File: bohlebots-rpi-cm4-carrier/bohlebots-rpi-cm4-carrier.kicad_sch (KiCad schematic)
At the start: 28 parts, among them J1 SI-46001-F, J2 power_reference, J3 IO_Conn_02x05, J4 I2C_Conn_1x04, K1 Kicker, T1 Taster_LED, T2 Taster_LED, U1 Compute_Module_4_Connectors, U2 USB_Conn_01x05_Pin, X1 Miromatch

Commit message: Added esd protection TODO: find fitting tvs diode (tht) 2p, 4p
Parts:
- added U2: TPD2EUSB30, Package_TO_SOT_SMD:Texas_DRT-3, symbol Power_Protection:TPD2EUSB30
- added U5: TPD4EUSB30, Package_SON:USON-10_2.5x1.0mm_P0.5mm, symbol CM4IO:TPD4EUSB30
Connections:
- net GND: now also U2.3 (GND), U5.3 (GND), U5.8 (GND)
- net USB_N: now also U2.2 (D-)
- net USB_P: now also U2.1 (D+)
- net USB_OTG: now reaches U1.101 (USB_OTG_ID)
- net USB_OTG: now also J3.9 (USB_OTG)
- net RUN_PG: no longer names the net of U1.92 (RUN_PG)
- net RUN_PG: no longer J3.9 (RUN_PG)
- new net TRD0_N: U5.4 (D2+), U5.7
- new net TRD0_P: U5.5 (D2-), U5.6
- new net TRD1_N: U5.2 (D1-), U5.9
- new net TRD1_P: U5.1 (D1+), U5.10
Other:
- note removed: "drive low with 220R to reset"
- moved on the sheet: J3, J4

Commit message: Added tsv diodes.
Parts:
- removed U2: TPD2EUSB30, Package_TO_SOT_SMD:Texas_DRT-3, symbol Power_Protection:TPD2EUSB30
- added U3: DT1446-04SO-7, bohlebots-rpi-cm4-carrier:SOT26, symbol CM4IO:TPD4EUSB30
- U5: value TPD4EUSB30 -> DT1446-04SO-7; footprint Package_SON:USON-10_2.5x1.0mm_P0.5mm -> bohlebots-rpi-cm4-carrier:SOT26; Hersteller (none) -> Diodes Incorporated
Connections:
- net TRD0_N is gone; now on net USB_N: U5.4 (D2+), U5.7
- net 5V: now also U5.5 (VCC)
- net GND: now also U5.2 (GND), U3.2 (GND), U3.8 (GND); no longer U5.3 (GND)
- net RD_N: now also U3.1 (D1-), U3.9
- net RD_P: now also U3.10, U3.6
- net TD_N: now also U3.3 (D2-), U3.6
- net TD_P: now also U3.4 (D2+), U3.7
- net USB_P: now also U5.3 (D2-), U5.6
- removed net TRD0_P: U5.5 (D2-), U5.6
- net TRD1_N: no longer names the net of U5.9
- net TRD1_N: now also U5.1 (D1-); no longer U5.2 (D1-)
- net TRD1_P: no longer names the net of U5.10
- net TRD1_P: now also U5.6; no longer U5.1 (D1+)
- net USB_OTG renamed USB_OTG_ID
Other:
- moved on the sheet: C1, ESCON1, ESCON2, ESCON3, ESCON4, J1, J3, J4, JP1, JP2, JP3, JP4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

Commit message: Started routing.
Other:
- moved on the sheet: C1, J1, U2, U3, U5

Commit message: PCB Layout Update.
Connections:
- net USB_N: now also U5.1 (D1-), U5.9; no longer U5.4 (D2+), U5.7
- net USB_P: now also U5.10; no longer U5.3 (D2-)
- new net: U5.3 (D2-), U5.6
- new net: U5.4 (D2+), U5.7
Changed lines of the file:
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@@
     (effects (font (size 1.27 1.27)) (justify right bottom))
-  )
-  (label "USB_N" (at 265.43 104.14 0) (fields_autoplaced)
-    (effects (font (size 1.27 1.27)) (justify left bottom))
   )
   (label "PWM3" (at 120.65 59.69 0) (fields_autoplaced)
@@
     (effects (font (size 1.27 1.27)) (justify left bottom))
   )
+  (label "USB_N" (at 231.14 109.22 0) (fields_autoplaced)
+    (effects (font (size 1.27 1.27)) (justify left bottom))
+  )
   (label "3.3v" (at 179.07 92.71 0) (fields_autoplaced)
     (effects (font (size 1.27 1.27)) (justify left bottom))
@@
   )
   (label "DIR3" (at 45.72 62.23 0) (fields_autoplaced)
-    (effects (font (size 1.27 1.27)) (justify left bottom))
-  )
-  (label "USB_P" (at 265.43 109.22 0) (fields_autoplaced)
     (effects (font (size 1.27 1.27)) (justify left bottom))
   )
@@
     (effects (font (size 1.27 1.27)) (justify left bottom))
   )
+  (label "USB_P" (at 231.14 104.14 0) (fields_autoplaced)
+    (effects (font (size 1.27 1.27)) (justify left bottom))
+  )

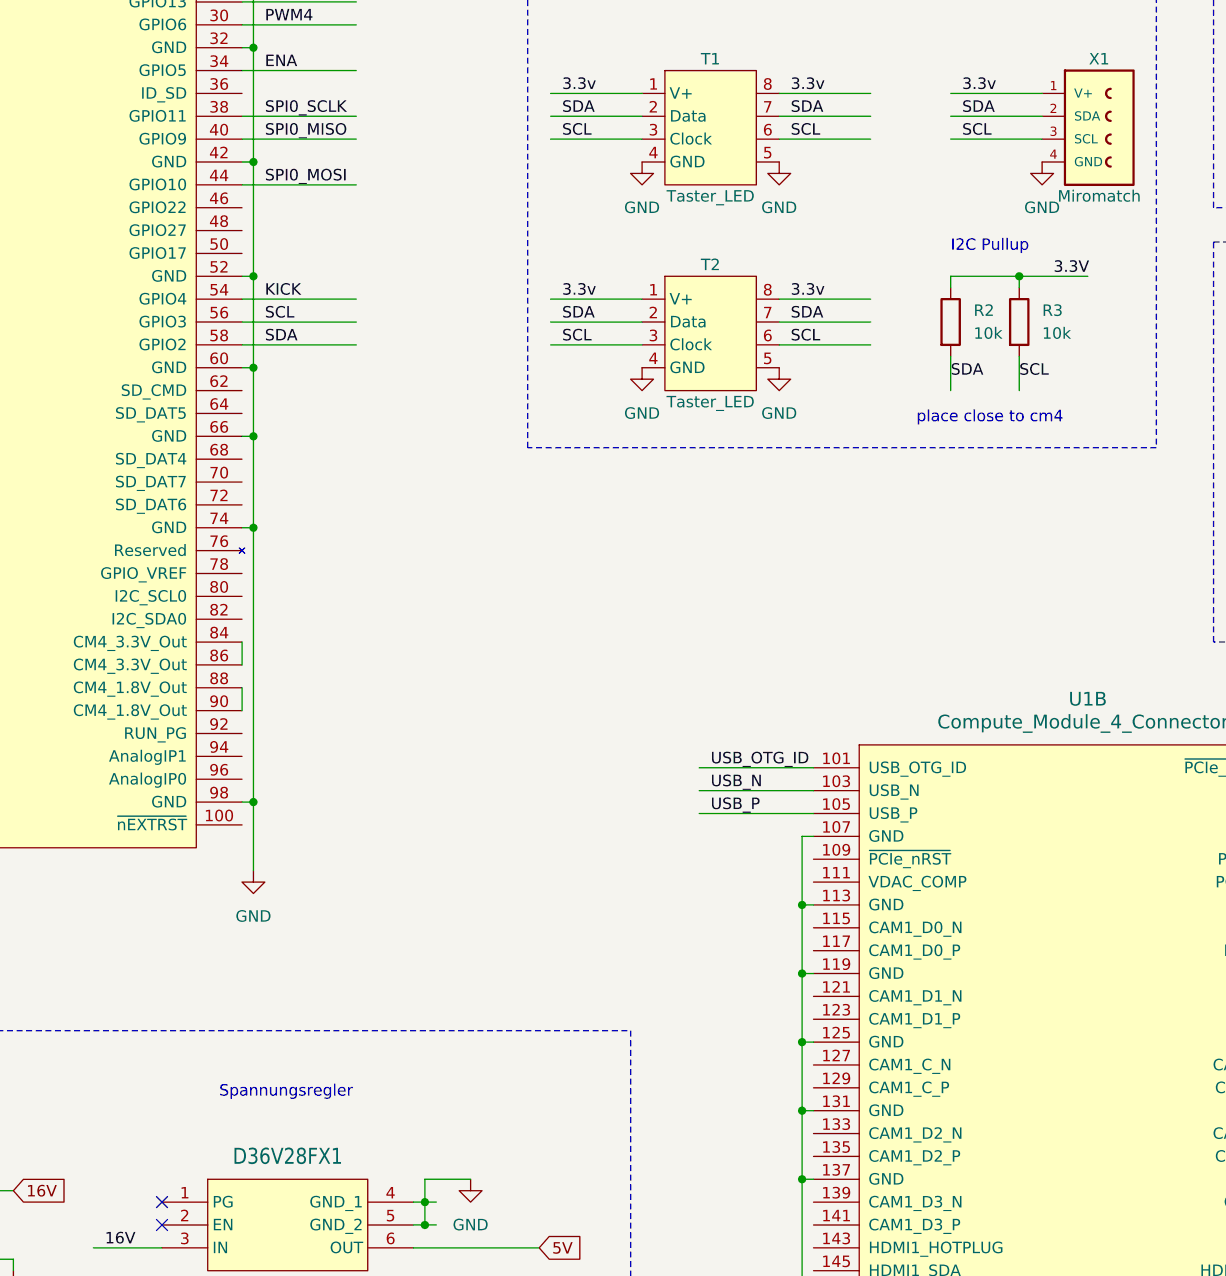
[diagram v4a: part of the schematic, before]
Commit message: Updated pcb layout.
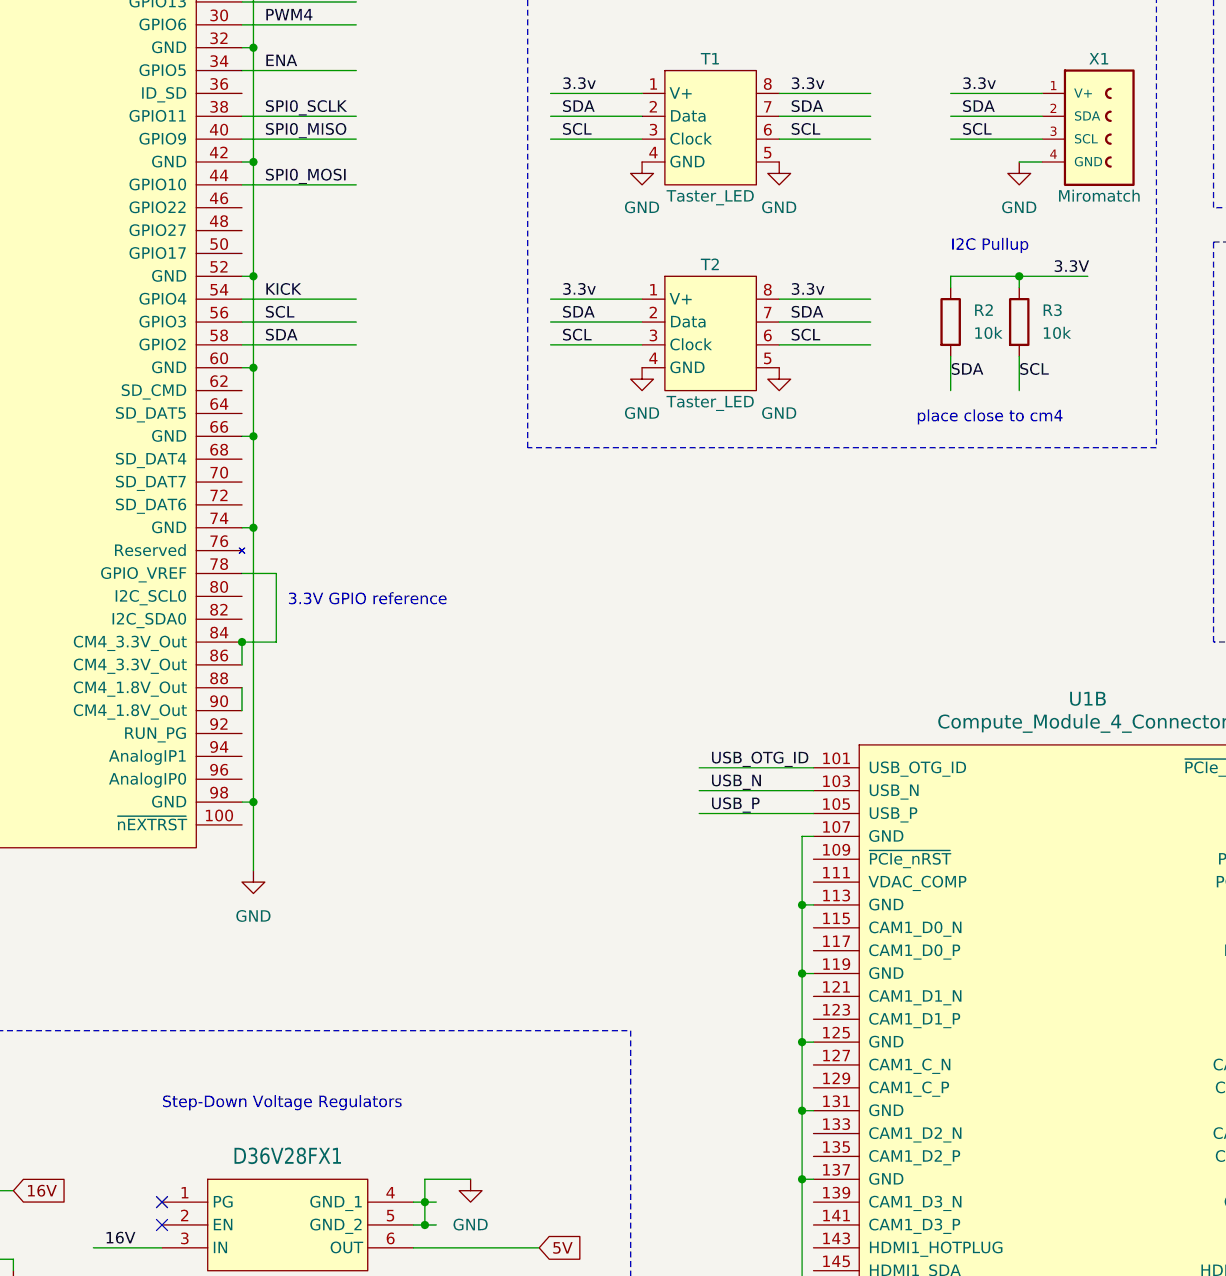
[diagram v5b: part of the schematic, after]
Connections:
- net at U1.78 (GPIO_VREF): now also U1.84 (CM4_3.3V_Out), U1.86 (CM4_3.3V_Out)
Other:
- note added: "3.3V GPIO reference"
- note added: "Step-Down Voltage Regulators"
- note removed: "Spannungsregler"
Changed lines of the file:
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@@
   (junction (at 243.84 259.08) (diameter 0) (color 0 0 0 0)
+  )
+  (junction (at 118.11 130.81) (diameter 0) (color 0 0 0 0)
   )
   (junction (at 138.43 214.63) (diameter 0) (color 0 0 0 0)
@@
     (stroke (width 0) (type default))
   )
+  (wire (pts (xy 118.11 123.19) (xy 121.92 123.19))
+    (stroke (width 0) (type default))
+  )
   (wire (pts (xy 55.88 92.71) (xy 57.15 92.71))
     (stroke (width 0) (type default))
@@
     (stroke (width 0) (type default))
   )
+  (wire (pts (xy 204.47 77.47) (xy 207.01 77.47))
+    (stroke (width 0) (type default))
+  )
   (wire (pts (xy 242.57 198.12) (xy 243.84 198.12))
     (stroke (width 0) (type default))
@@
   )
   (wire (pts (xy 44.45 95.25) (xy 57.15 95.25))
+    (stroke (width 0) (type default))
+  )
+  (wire (pts (xy 121.92 130.81) (xy 118.11 130.81))
     (stroke (width 0) (type default))
   )
@@
   )
   (wire (pts (xy 168.91 147.32) (xy 181.61 147.32))
+    (stroke (width 0) (type default))
+  )
+  (wire (pts (xy 121.92 123.19) (xy 121.92 130.81))
     (stroke (width 0) (type default))
   )
@@
     (effects (font (size 1.27 1.27)) (justify left bottom))
   )
-  (text "Spannungsregler" (at 115.57 181.61 0)
+  (text "Step-Down Voltage Regulators" (at 109.22 182.88 0)
     (effects (font (size 1.27 1.27)) (justify left bottom))
   )
   (text "Additional I2C\n   breakout" (at 284.48 198.12 0)
+    (effects (font (size 1.27 1.27)) (justify left bottom))
+  )
+  (text "3.3V GPIO reference" (at 123.19 127 0)
     (effects (font (size 1.27 1.27)) (justify left bottom))
   )
@@
     )
   )
-  (symbol (lib_id "power:GND") (at 207.01 77.47 0) (unit 1)
+  (symbol (lib_id "power:GND") (at 204.47 77.47 0) (unit 1)
     (in_bom yes) (on_board yes) (dnp no) (fields_autoplaced)
-    (property "Reference" "#PWR09" (at 207.01 83.82 0)
-      (effects (font (size 1.27 1.27)) hide)
-    )
-    (property "Value" "GND" (at 207.01 82.55 0)
+    (property "Reference" "#PWR09" (at 204.47 83.82 0)
+      (effects (font (size 1.27 1.27)) hide)
+    )
+    (property "Value" "GND" (at 204.47 82.55 0)
       (effects (font (size 1.27 1.27)))
     )
-    (property "Footprint" "" (at 207.01 77.47 0)
-      (effects (font (size 1.27 1.27)) hide)
-    )
-    (property "Datasheet" "" (at 207.01 77.47 0)
-      (effects (font (size 1.27 1.27)) hide)
-    )
+    (property "Footprint" "" (at 204.47 77.47 0)
+      (effects (font (size 1.27 1.27)) hide)
+    )
+    (property "Datasheet" "" (at 204.47 77.47 0)
+      (effects (font (size 1.27 1.27)) hide)
+    )

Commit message: IC placement done.
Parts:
- removed H1: Pinhead_1x04V, bohlebots:PinHeader_1x04_P2.54mm_Vertical, symbol bohlebots.lib:Pinhead_1x04V
- added J5, J6: pwr_connector, Connector_PinHeader_2.54mm:PinHeader_1x03_P2.54mm_Vertical, symbol Connector_Generic:Conn_01x03
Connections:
- net 16V: now also J5.1 (VCC)
- net GND: now also J6.3 (GND)
- new net: J5.3 (GND), J6.1 (VCC)
- no-connect marks 11 -> 9
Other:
- note added: "Akku A"
- note added: "Akku B"
- note added: "ESD Schutz"
- note removed: "test voltage or connect voltmeter display"
- moved on the sheet: C2, J2

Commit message: V01 finished.
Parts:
- added U4: DT1446-04SO-7, bohlebots-rpi-cm4-carrier:SOT26, symbol CM4IO:TPD4EUSB30
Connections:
- net 3.3v is gone; now on net 3.3V: T1.1 (V+), T1.8, T2.1 (V+), T2.8, X1.1 (V+)
- net DIR1: no longer ESCON2.P15 (D3), ESCON3.P15 (D3), ESCON4.P15 (D3)
- net DIR2: now also ESCON2.P15 (D3)
- net DIR3: now also ESCON3.P15 (D3)
- net DIR4: now also ESCON4.P15 (D3)
- net GND: now also U4.2 (GND); no longer U3.8 (GND), U5.8 (GND)
- net PWM1: no longer ESCON2.P17 (D1), ESCON3.P17 (D1), ESCON4.P17 (D1)
- net PWM2: now also ESCON2.P17 (D1)
- net PWM3: now also ESCON3.P17 (D1)
- net PWM4: now also ESCON4.P17 (D1)
- net RD_N: now also U4.3 (D2-), U4.4 (D2+); no longer U3.1 (D1-), U3.9
- net RD_P: now also U4.1 (D1-), U4.6 (D1+); no longer U3.10, U3.6
- net TD_N: now also U3.4 (D2+); no longer U3.6
- net TD_P: now also U3.1 (D1-), U3.6 (D1+); no longer U3.4 (D2+), U3.7
- net USB_N: now also U5.3 (D2-), U5.4 (D2+); no longer U5.1 (D1-), U5.9
- net USB_P: now also U5.1 (D1-); no longer U5.10
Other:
- moved on the sheet: C1, J1, U2, U3, U5

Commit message: V01.2 Update.
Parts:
- added U6: DT1446-04SO-7, bohlebots-rpi-cm4-carrier:SOT26, symbol CM4IO:TPD4EUSB30
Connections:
- net 3.3V: now also U6.5 (VCC)
- net GND: now also U6.2 (GND)
- net SCL: now also U6.3 (D2-), U6.4 (D2+)
- net SDA: now also U6.1 (D1-), U6.6 (D1+)
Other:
- moved on the sheet: R2, R3, T1, T2, X1
